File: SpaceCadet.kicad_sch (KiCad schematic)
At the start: 37 parts, among them J1 USB_C_Receptacle_USB2.0_16P, J2 Conn_01x04, J3 Conn_01x05, U1 RP2040, U2 XC6206PxxxMR, U3 SRV05-4, U4 W25Q128JVS, Y1 Crystal_GND24

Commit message: wip: rpi-pico added
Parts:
- removed BOOT1, RST1: SW_Push, Button_Switch_SMD:SW_SPST_TL3342, symbol Switch:SW_Push
- removed C1, C2, C5, C6, C9: 1u, Capacitor_SMD:C_0402_1005Metric, symbol Device:C_Small
- removed C10, C11, C12, C13, C14, C15, C16, C7: 100n, Capacitor_SMD:C_0402_1005Metric, symbol Device:C_Small
- removed C20, C21: 22p, Capacitor_SMD:C_0402_1005Metric, symbol Device:C_Small
- removed C8: 10u, Capacitor_SMD:C_0603_1608Metric, symbol Device:C_Small
- removed F17: Fuse_Small, Fuse:Fuse_1206_3216Metric, symbol Device:Fuse_Small
- removed J1: USB_C_Receptacle_USB2.0_16P, Connector_USB:USB_C_Receptacle_HRO_TYPE-C-31-M-12, symbol Connector:USB_C_Receptacle_USB2.0_16P
- removed J2: Conn_01x04, Connector_JST:JST_SH_SM04B-SRSS-TB_1x04-1MP_P1.00mm_Horizontal, symbol Connector_Generic:Conn_01x04
- removed J3: Conn_01x05, Connector_PinHeader_2.54mm:PinHeader_1x05_P2.54mm_Vertical, symbol Connector_Generic:Conn_01x05
- removed R1, R2, R3, R4, R5: 5.1k, Resistor_SMD:R_0402_1005Metric, symbol Device:R_Small
- removed R6, R7: 1k, Resistor_SMD:R_0402_1005Metric, symbol Device:R_Small
- removed R94, R95: 27, Resistor_SMD:R_0402_1005Metric, symbol Device:R_Small
- removed U1: RP2040, Package_DFN_QFN:QFN-56-1EP_7x7mm_P0.4mm_EP3.2x3.2mm, symbol MCU_RaspberryPi:RP2040
- removed U2: XC6206PxxxMR, Package_TO_SOT_SMD:SOT-23-3, symbol Regulator_Linear:XC6206PxxxMR
- removed U3: SRV05-4, Package_TO_SOT_SMD:SOT-23-6, symbol Power_Protection:SRV05-4
- removed U4: W25Q128JVS, Package_SO:SOIC-8_5.23x5.23mm_P1.27mm, symbol Memory_Flash:W25Q128JVS
- removed Y1: Crystal_GND24, Crystal:Crystal_SMD_3225-4Pin_3.2x2.5mm_HandSoldering, symbol Device:Crystal_GND24
- added U101: Pico, RPI:RPi_Pico_SMD_TH, symbol RPI:Pico
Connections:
- no-connect marks 2 -> 0
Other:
- moved on the sheet: DISPLAY1

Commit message: wip: schematic refactor
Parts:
- U101: footprint RPI:RPi_Pico_SMD_TH -> RPi_Pico:RPi_Pico_SMD_TH
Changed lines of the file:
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@@
 			)
 		)
-		(property "Footprint" "RPI:RPi_Pico_SMD_TH"
+		(property "Footprint" "RPi_Pico:RPi_Pico_SMD_TH"
 			(at 234.061 192.024 90)
 			(effects

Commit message: upd: RPI footprint
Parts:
- U101: footprint RPi_Pico:RPi_Pico_SMD_TH -> Button_Switch_Keyboard:RPi_Pico_SMD_TH
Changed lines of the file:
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@@
 			)
 		)
-		(property "Footprint" "RPi_Pico:RPi_Pico_SMD_TH"
+		(property "Footprint" "Button_Switch_Keyboard:RPi_Pico_SMD_TH"
 			(at 234.061 192.024 90)
 			(effects

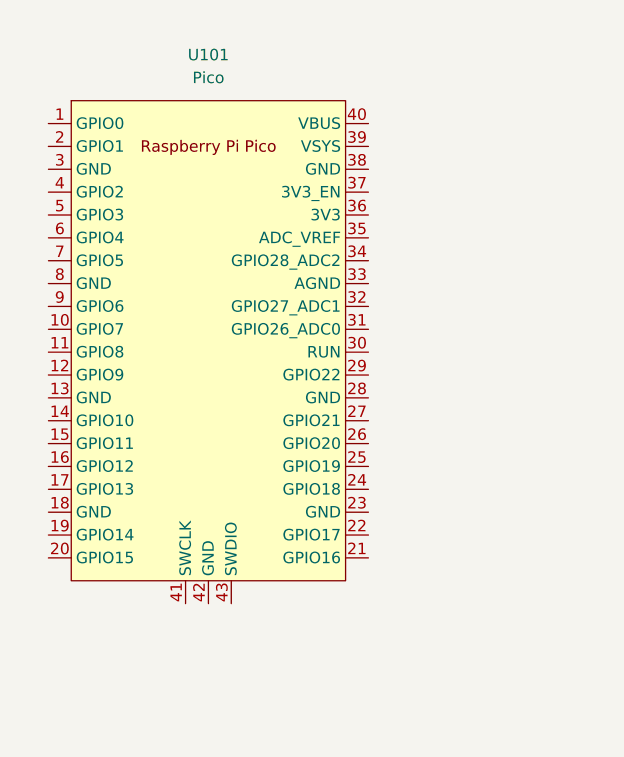
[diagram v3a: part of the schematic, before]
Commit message: imp: vcc & gnd added
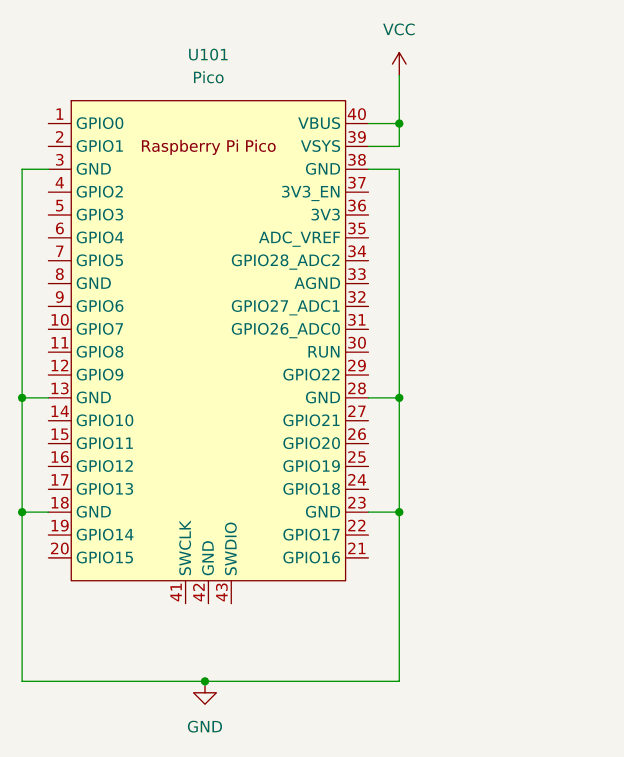
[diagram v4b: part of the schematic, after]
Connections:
- net GND: now reaches U101.13 (GND)
- net GND: now also U101.18 (GND), U101.23 (GND), U101.28 (GND), U101.3 (GND), U101.38 (GND)
- net VCC: now reaches U101.39 (VSYS)
- net VCC: now also U101.40 (VBUS)

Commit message: wip: rpi pico on pcb
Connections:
- net GND: no longer U101.13 (GND), U101.18 (GND), U101.23 (GND), U101.28 (GND), U101.3 (GND), U101.38 (GND)
- net COL9: now reaches U101.10 (GPIO7)
- net COL8: now reaches U101.11 (GPIO8)
- net COL7: now reaches U101.12 (GPIO9)
- net COL6: now reaches U101.14 (GPIO10)
- net COL5: now reaches U101.15 (GPIO11)
- net COL4: now reaches U101.16 (GPIO12)
- net COL3: now reaches U101.17 (GPIO13)
- net COL2: now reaches U101.19 (GPIO14)
- net COL1: now reaches U101.20 (GPIO15)
- net ROW6: now reaches U101.21 (GPIO16)
- net ROW7: now reaches U101.22 (GPIO17)
- net ROW5: now reaches U101.24 (GPIO18)
- net ROW8: now reaches U101.25 (GPIO19)
- net ROW4: now reaches U101.26 (GPIO20)
- net ROW9: now reaches U101.27 (GPIO21)
- net ROW3: now reaches U101.29 (GPIO22)
- net ROW10: now reaches U101.31 (GPIO26_ADC0)
- net ROW2: now reaches U101.32 (GPIO27_ADC1)
- net ROW1: now reaches U101.34 (GPIO28_ADC2)
- net COL11: now reaches U101.7 (GPIO5)
- net COL10: now reaches U101.9 (GPIO6)

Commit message: wip: pri fully connected with test points
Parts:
- added TP101, TP102, TP103, TP104, TP105, TP106, TP107, TP108, TP109, TP110, TP111, TP112, TP113, TP114: TestPoint, TestPoint:TestPoint_THTPad_2.0x2.0mm_Drill1.0mm, symbol Connector:TestPoint
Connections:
- net GND: now also U101.13 (GND), U101.18 (GND), U101.23 (GND), U101.28 (GND), U101.3 (GND), U101.33 (AGND), U101.38 (GND), U101.8 (GND), TP101.1
- net VCC: now also TP102.1
- net at U101.1 (GPIO0): now also TP103.1
- net at U101.2 (GPIO1): now also TP104.1
- net at U101.30 (RUN): now also TP111.1
- net at U101.35 (ADC_VREF): now also TP110.1
- net at U101.36 (3V3): now also TP109.1
- net at U101.37 (3V3_EN): now also TP108.1
- net at U101.4 (GPIO2): now also TP105.1
- net at U101.41 (SWCLK): now also TP112.1
- net at U101.42 (GND): now also TP113.1
- net at U101.43 (SWDIO): now also TP114.1
- net at U101.5 (GPIO3): now also TP106.1
- net at U101.6 (GPIO4): now also TP107.1
